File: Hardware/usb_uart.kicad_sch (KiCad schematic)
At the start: 15 parts, among them J2 USB_C_Receptacle_USB2.0, J3 USB_C_Receptacle_USB2.0, U4 CP2102N-Axx-xQFN28

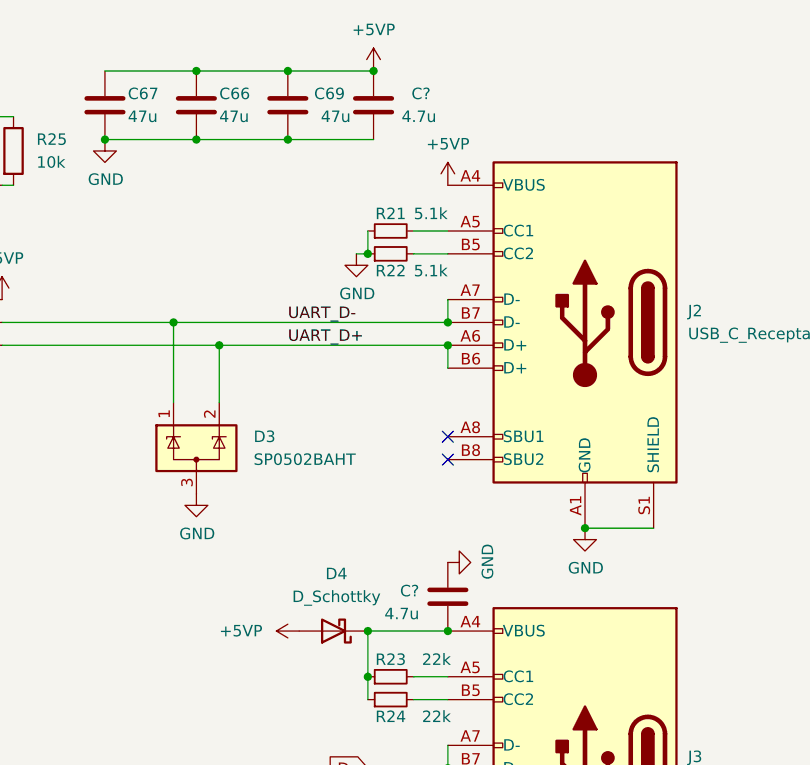
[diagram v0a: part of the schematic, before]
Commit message: fixed crystal resonator value
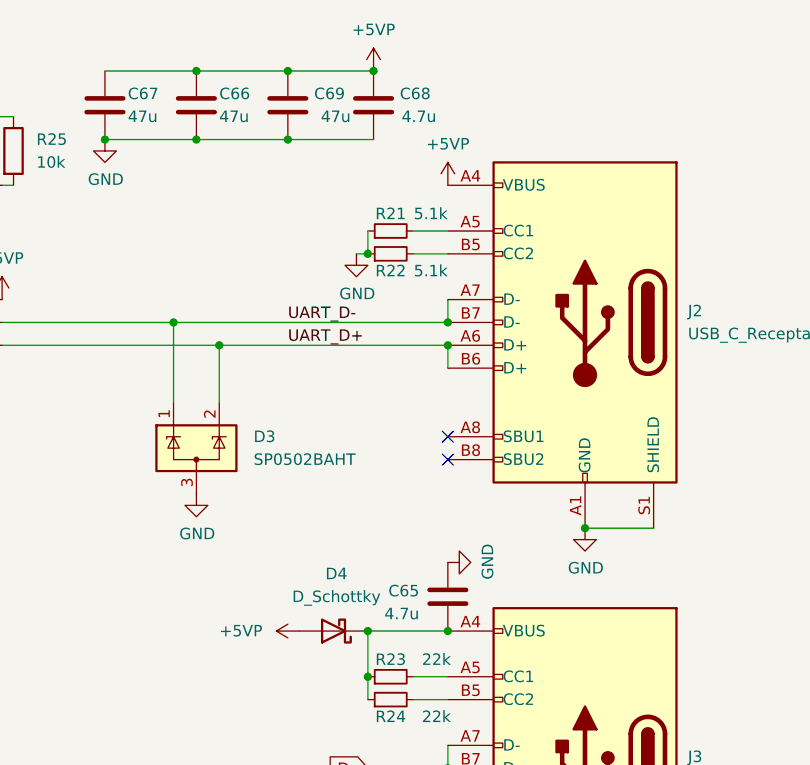
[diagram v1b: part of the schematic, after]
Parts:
- gave numbers to parts that had none: 2
